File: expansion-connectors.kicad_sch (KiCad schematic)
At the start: 6 parts, among them J10 LSHM-130-01-L-RH-A-S-K-TR

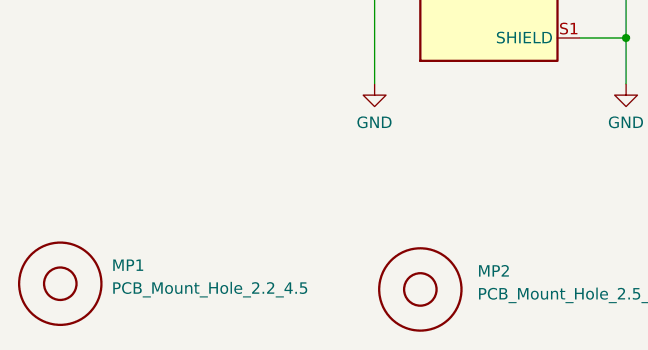
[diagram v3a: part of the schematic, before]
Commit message: [#46875] Update schematic symbols
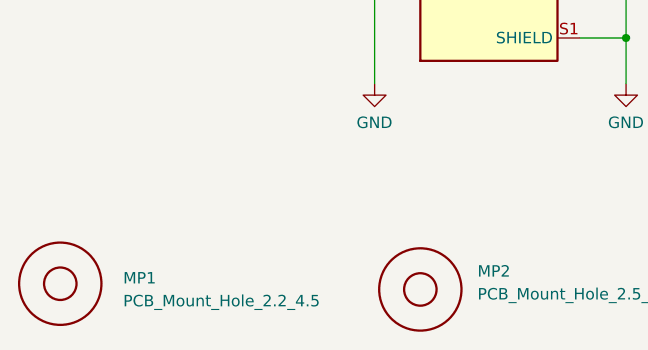
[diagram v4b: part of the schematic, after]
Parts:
- MP1, MP2, MP3: now left out of the parts list
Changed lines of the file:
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@@
   )
   (text "LSHM connector current rating:\n2A per pin (2 pins powered)"
-    (at 245.11 82.55 0)
+    (at 245.11 82.55 180)
     (effects (font (size 1.27 1.27)) (justify right bottom))
   )
@@
   )
   (symbol (lib_id "antmicroMechanicalParts:PCB_Mount_Hole_2.2_4.5") (at 135.255 196.215 0) (unit 1)
-    (in_bom yes) (on_board yes) (fields_autoplaced)
-    (property "Reference" "MP1" (id 0) (at 140.97 194.9449 0)
-      (effects (font (size 1.27 1.27) (thickness 0.15)) (justify left bottom))
-    )
-    (property "Value" "PCB_Mount_Hole_2.2_4.5" (id 1) (at 140.97 197.4849 0)
+    (in_bom no) (on_board yes) (fields_autoplaced)
+    (property "Reference" "MP1" (id 0) (at 142.24 196.3411 0)
+      (effects (font (size 1.27 1.27) (thickness 0.15)) (justify left bottom))
+    )
+    (property "Value" "PCB_Mount_Hole_2.2_4.5" (id 1) (at 142.24 198.8811 0)
       (effects (font (size 1.27 1.27) (thickness 0.15)) (justify left bottom))
     )
@@
     )
   )
-  (symbol (lib_id "antmicroMechanicalParts:PCB_Mount_Hole_2.5_6.2") (at 175.26 196.85 0) (unit 1)
-    (in_bom yes) (on_board yes) (fields_autoplaced)
+  (symbol (lib_name "PCB_Mount_Hole_2.5_6.2_2") (lib_id "antmicroMechanicalParts:PCB_Mount_Hole_2.5_6.2") (at 175.26 196.85 0) (unit 1)
+    (in_bom no) (on_board yes) (fields_autoplaced)
     (property "Reference" "MP2" (id 0) (at 181.61 195.5799 0)
       (effects (font (size 1.27 1.27) (thickness 0.15)) (justify left bottom))
@@
   )
   (symbol (lib_id "antmicroMechanicalParts:PCB_Mount_Hole_2.5_6.2") (at 213.36 196.85 0) (unit 1)
-    (in_bom yes) (on_board yes) (fields_autoplaced)
+    (in_bom no) (on_board yes) (fields_autoplaced)
     (property "Reference" "MP3" (id 0) (at 219.71 195.5799 0)
       (effects (font (size 1.27 1.27) (thickness 0.15)) (justify left bottom))

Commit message: [#46875] Update Mount-hole-M2.5
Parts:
- MP2, MP3: footprint antmicro-footprints:Mount-hole-M2.5 -> antmicro-footprints:mounting-hole-2.75mm-M2.5_D6.2mm_PTH
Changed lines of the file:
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@@
       (effects (font (size 1.27 1.27) (thickness 0.15)) (justify left bottom))
     )
-    (property "Footprint" "antmicro-footprints:Mount-hole-M2.5" (id 2) (at 193.04 204.47 0)
+    (property "Footprint" "antmicro-footprints:mounting-hole-2.75mm-M2.5_D6.2mm_PTH" (id 2) (at 193.04 204.47 0)
       (effects (font (size 1.27 1.27) (thickness 0.15)) (justify left bottom) hide)
     )
@@
       (effects (font (size 1.27 1.27) (thickness 0.15)) (justify left bottom))
     )
-    (property "Footprint" "antmicro-footprints:Mount-hole-M2.5" (id 2) (at 231.14 204.47 0)
+    (property "Footprint" "antmicro-footprints:mounting-hole-2.75mm-M2.5_D6.2mm_PTH" (id 2) (at 231.14 204.47 0)
       (effects (font (size 1.27 1.27) (thickness 0.15)) (justify left bottom) hide)
     )

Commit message: [#46875] kmake loclib
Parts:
- J10: footprint antmicro-footprints:SAMTEC_LSHM-130-01-XXX-RH-A-S-K-XX -> scalenode-cm4-baseboard-footprints:SAMTEC_LSHM-130-01-XXX-RH-A-S-K-XX; symbol antmicroB2bConnectors:LSHM-130-01-L-RH-A-S-K-TR -> scalenode-cm4-baseboard:LSHM-130-01-L-RH-A-S-K-TR
- MP1: footprint antmicro-footprints:mounting-hole-2.2mm -> scalenode-cm4-baseboard-footprints:mounting-hole-2.2mm; symbol antmicroMechanicalParts:PCB_Mount_Hole_2.2_4.5 -> scalenode-cm4-baseboard:PCB_Mount_Hole_2.2_4.5
- MP2, MP3: footprint antmicro-footprints:mounting-hole-2.75mm-M2.5_D6.2mm_PTH -> scalenode-cm4-baseboard-footprints:mounting-hole-2.75mm-M2.5_D6.2mm_PTH; symbol antmicroMechanicalParts:PCB_Mount_Hole_2.5_6.2 -> scalenode-cm4-baseboard:PCB_Mount_Hole_2.5_6.2
- R62, R63: footprint antmicro-footprints:R_1206_3216Metric -> scalenode-cm4-baseboard-footprints:R_1206_3216Metric; symbol antmicroResistorsmisc:R_0R_1206 -> scalenode-cm4-baseboard:R_0R_1206

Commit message: [#46875] Revert kmake loclib
This reverts commit a23b923226223a7ebbdda1690aa69773ccaf4a95.
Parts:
- J10: footprint scalenode-cm4-baseboard-footprints:SAMTEC_LSHM-130-01-XXX-RH-A-S-K-XX -> antmicro-footprints:SAMTEC_LSHM-130-01-XXX-RH-A-S-K-XX; symbol scalenode-cm4-baseboard:LSHM-130-01-L-RH-A-S-K-TR -> antmicroB2bConnectors:LSHM-130-01-L-RH-A-S-K-TR
- MP1: footprint scalenode-cm4-baseboard-footprints:mounting-hole-2.2mm -> antmicro-footprints:mounting-hole-2.2mm; symbol scalenode-cm4-baseboard:PCB_Mount_Hole_2.2_4.5 -> antmicroMechanicalParts:PCB_Mount_Hole_2.2_4.5
- MP2, MP3: footprint scalenode-cm4-baseboard-footprints:mounting-hole-2.75mm-M2.5_D6.2mm_PTH -> antmicro-footprints:mounting-hole-2.75mm-M2.5_D6.2mm_PTH; symbol scalenode-cm4-baseboard:PCB_Mount_Hole_2.5_6.2 -> antmicroMechanicalParts:PCB_Mount_Hole_2.5_6.2
- R62, R63: footprint scalenode-cm4-baseboard-footprints:R_1206_3216Metric -> antmicro-footprints:R_1206_3216Metric; symbol scalenode-cm4-baseboard:R_0R_1206 -> antmicroResistorsmisc:R_0R_1206
